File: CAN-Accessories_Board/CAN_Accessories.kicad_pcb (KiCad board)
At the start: 2 copper layers, 83.8 x 63.5 mm, 47 parts, among them J1 39301040, J2 39301040, J3 39301040, J4 39301040, J5 39301040, J6 39301040, J7 39301060, J8 39301060, Q1 Q_NMOS_SGD, Q2 Q_NMOS_SGD, Q3 Q_NMOS_SGD, Q4 Q_NMOS_SGD, Q5 Q_NMOS_SGD, Q6 Q_NMOS_SGD, U1 NUCLEO_L432KC, U2 MCP2562FD-E_SN

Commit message: Changed layout
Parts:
- added R14: 10K, Resistor_SMD:R_0603_1608Metric, B.Cu at (88.7, 122.0)
- added R15: 10K, Resistor_SMD:R_0603_1608Metric, B.Cu at (85.2, 122.0)
- added R16: 10K, Resistor_SMD:R_0603_1608Metric, B.Cu at (81.8, 122.0)
- moved J7 52.8 mm to (53.5, 104.1), turned to 90 degrees
- moved J8 52.8 mm to (53.5, 124.4), turned to 90 degrees
- moved JP1 25.2 mm to (88.7, 119.3)
- moved JP2 25.0 mm to (85.3, 119.3)
- moved JP3 24.7 mm to (82.0, 119.3)
- moved U1 23.9 mm to (92.2, 118.2)
- moved D6 23.8 mm to (69.7, 122.2)
- moved R9 23.8 mm to (75.3, 121.4)
- moved D1 23.8 mm to (117.9, 122.0)
- moved D2 23.8 mm to (110.4, 121.9)
- moved D3 23.8 mm to (102.9, 121.9)
- moved D4 23.8 mm to (95.4, 121.9)
- moved D5 23.8 mm to (78.0, 122.2)
- moved Q1 23.8 mm to (116.2, 116.2)
- moved Q2 23.8 mm to (108.8, 116.2)
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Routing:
- net Net-(F4-Pad2): track 21.4 -> 72.1 mm, vias 2 -> 1
- net /5V: track 33.5 -> 77.6 mm, vias 2 -> 1
- net /STBY: track 9.82 -> 42.5 mm
- net /3V3: track 88.0 -> 60.3 mm, vias 1 -> 0
- net Net-(F3-Pad2): track 19.6 -> 46.6 mm, vias 2 -> 1
- net /CANRX: track 33.0 -> 9.65 mm
- net GND: track 18.5 -> 41.7 mm
- net Net-(F6-Pad1): track 17.6 -> 33.0 mm
- net /CANTX: track 12.1 -> 27.0 mm
- net Net-(F1-Pad1): track 32.7 -> 18.0 mm
- net Net-(F2-Pad1): track 28.9 -> 17.9 mm
- net Net-(F5-Pad1): track 17.7 -> 28.3 mm
- net Net-(F5-Pad2): track 18.7 -> 28.4 mm, vias 2 -> 1
- net +12V: track 33.6 -> 27.4 mm
- net Net-(F3-Pad1): track 25.0 -> 20.7 mm
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
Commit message: Changed PCB Layout
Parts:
- moved D4 0.76 mm to (96.2, 121.9)
- moved R7 0.76 mm to (93.5, 121.1)
- moved R8 0.76 mm to (93.5, 123.1)
- moved D3 0.40 mm to (103.3, 121.8)
- moved R5 0.40 mm to (100.6, 121.0)
- moved R6 0.40 mm to (100.6, 122.9)

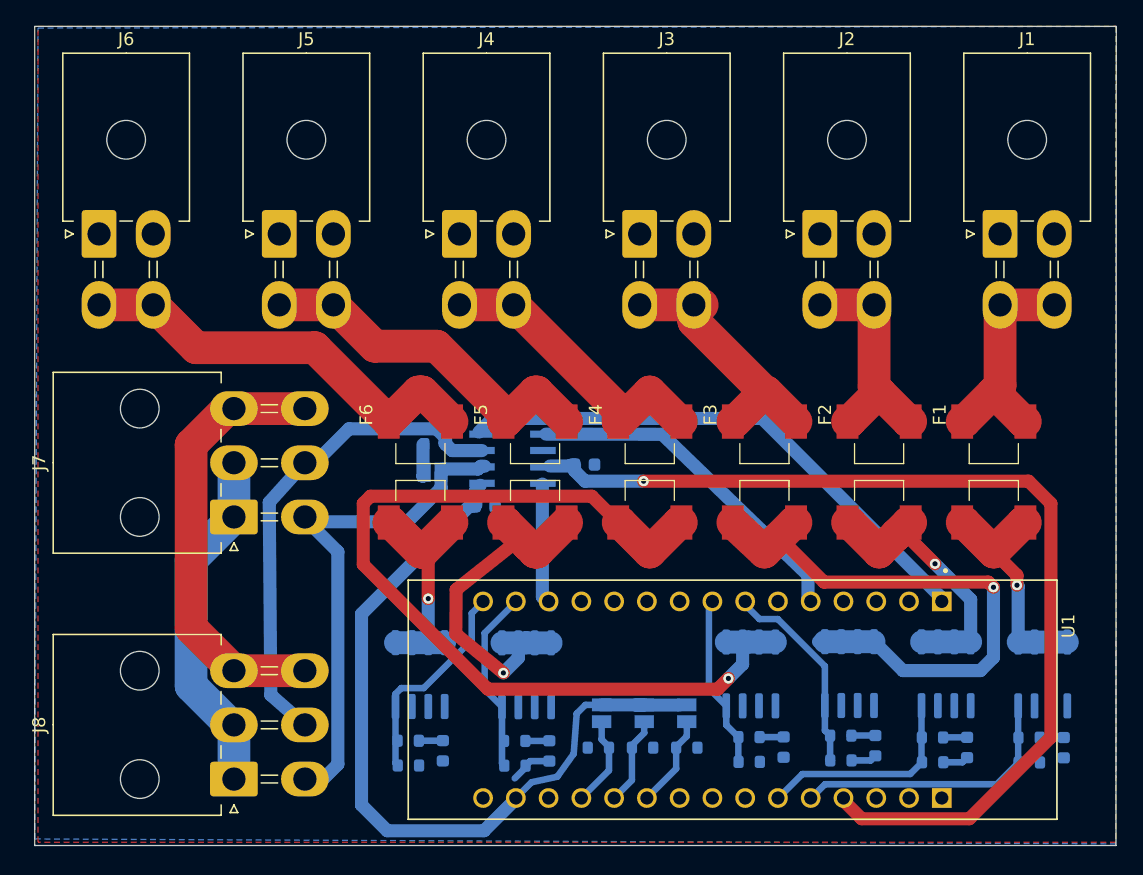
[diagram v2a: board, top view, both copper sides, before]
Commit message: Changed footprints from 0603 to 0805
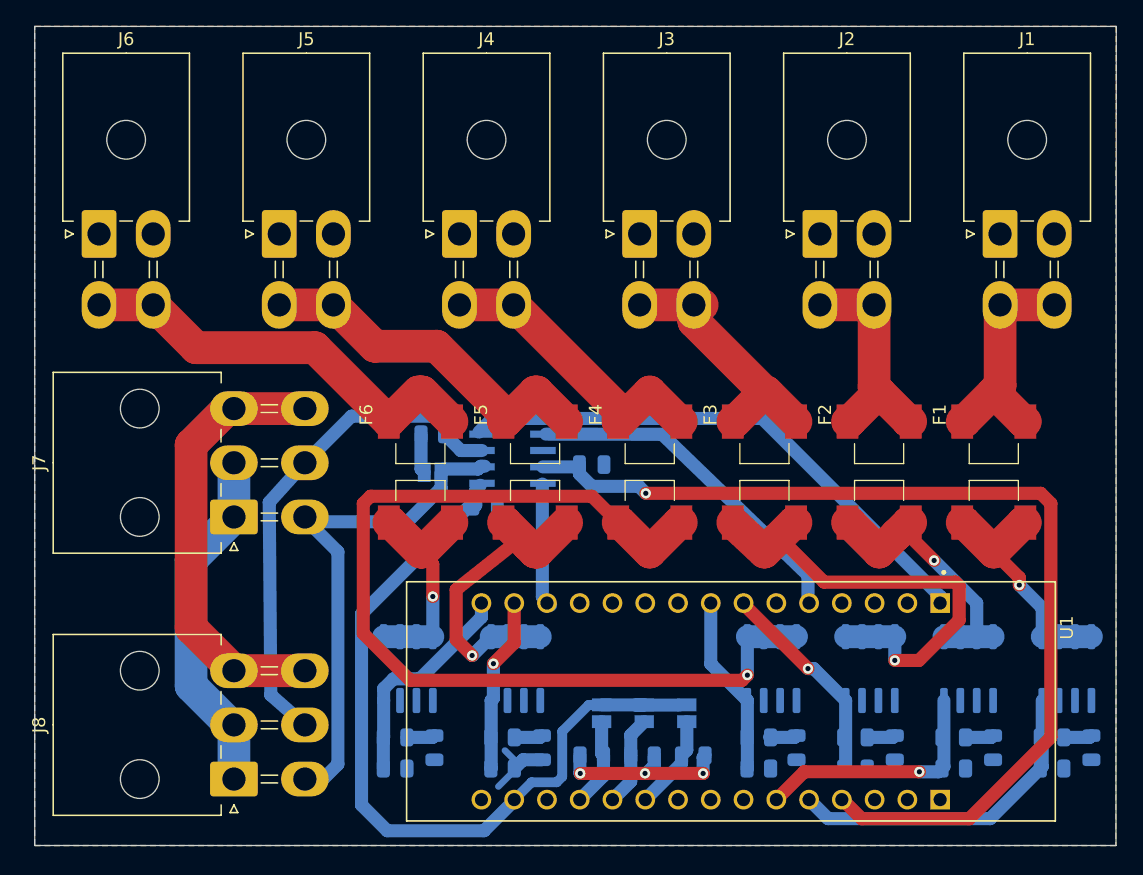
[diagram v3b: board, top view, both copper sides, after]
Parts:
- C1, C2: footprint Capacitor_SMD:C_0603_1608Metric -> Capacitor_SMD:C_0805_2012Metric
- D1, D2, D3, D4, D5, D6: footprint LED_SMD:LED_0603_1608Metric -> LED_SMD:LED_0805_2012Metric
- R1, R10, R11, R12, R13, R14, R15, R16, R2, R3, R4, R5, R6, R7, R8, R9: footprint Resistor_SMD:R_0603_1608Metric -> Resistor_SMD:R_0805_2012Metric
- moved D1 2.14 mm to (120.0, 122.0)
- moved D2 2.02 mm to (112.4, 122.0)
- moved Q1 1.91 mm to (118.1, 115.8)
- moved R2 1.82 mm to (117.0, 123.6)
- moved Q2 1.78 mm to (110.5, 115.8)
- moved R1 1.78 mm to (117.0, 121.2)
- moved R4 1.71 mm to (109.3, 123.6)
- moved Q4 1.69 mm to (95.2, 115.8)
- moved Q3 1.66 mm to (102.9, 115.8)
- moved R3 1.65 mm to (109.3, 121.2)
- moved D3 1.52 mm to (104.8, 122.0)
- moved R6 1.29 mm to (101.7, 123.6)
- moved R5 1.15 mm to (101.7, 121.2)
- moved R12 1.06 mm to (66.0, 123.6)
- moved R11 1.05 mm to (66.0, 121.2)
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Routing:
- net GND: track 41.7 -> 54.4 mm, vias 0 -> 3
- net Net-(F3-Pad2): track 46.6 -> 36.9 mm
- net Net-(F4-Pad2): track 72.1 -> 75.9 mm
- net /GATE1: track 21.8 -> 25.5 mm
- net Net-(F5-Pad2): track 28.4 -> 25.1 mm
- net /GATE2: track 16.9 -> 19.2 mm, vias 0 -> 1
- net /CANH: track 38.2 -> 39.3 mm
- net /5V: track 77.6 -> 78.6 mm
- net /GATE4: track 13.3 -> 14.3 mm
- net /GATE6: track 16.4 -> 17.2 mm
- net /GATE5: track 14.2 -> 13.6 mm, vias 0 -> 1
- net /3V3: track 60.3 -> 60.9 mm
- net /GATE3: track 15.8 -> 16.4 mm, vias 0 -> 1
- net Net-(JP4-Pad1): track 2.48 -> 3.05 mm
- net Net-(F6-Pad2): track 17.9 -> 18.4 mm
